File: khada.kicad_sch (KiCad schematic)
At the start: 52 parts, among them J1 MJ-4PP-9, SW1 SW_Push, SW10 SW_Push, SW11 SW_Push, SW12 SW_Push, SW13 SW_Push, SW14 SW_Push, SW15 SW_Push, SW16 SW_Push, SW17 SW_Push, SW18 SW_Push, SW19 SW_Push, SW2 SW_Push, SW20 SW_Push, SW21 SW_Push, SW22 SW_Push, SW3 SW_Push, SW4 SW_Push, SW5 SW_Push, SW6 SW_Push, SW7 SW_Push, SW8 SW_Push, SW9 SW_Push, U1 YAAJ_WeAct_BlackPill_Part_Lik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

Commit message: final design unless wiring incorrect
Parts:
- SW1, SW10, SW12, SW13, SW14, SW15, SW16, SW17, SW18, SW19, SW2, SW20, SW21, SW22, SW3, SW4, SW5: footprint MX_Only:MXOnly-1U-NoLED -> switches:SW_MX_reversible_NoSilk
- SW11, SW6, SW7, SW8, SW9: footprint mx_only:MXOnly-1U-NoLED -> switches:SW_MX_reversible_NoSilk

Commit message: added encoder
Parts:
- added D23: D_Small, acheron_Components:D_THT_7.62mm_copy, symbol Device:D_Small
- added SW23: RotaryEncoder_Switch, keebio:RotaryEncoder_Alps_EC11E-Switch_Vertical_H20mm, symbol Device:RotaryEncoder_Switch
- renumbered D9 to D10, D14 to D11, D11 to D12, D12 to D13, D13 to D14, D18 to D15, D15 to D16, D16 to D17, D17 to D18, D22 to D19, D19 to D20, D20 to D21, D21 to D22, D10 to D7, D7 to D8, D8 to D9, SW9 to SW10, SW14 to SW11, SW11 to SW12, SW12 to SW13, SW13 to SW14, SW18 to SW15, SW15 to SW16, SW16 to SW17, SW17 to SW18, SW22 to SW19, SW19 to SW20, SW20 to SW21, SW21 to SW22, SW10 to SW7, SW7 to SW8, SW8 to SW9
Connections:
- net +5V: now also R1.1; no longer R1.2
- net DATA: now also J1.B, R1.2, U1.10 (PA15); no longer J1.A, R1.1, U1.17 (PB9)
- net GND: now also SW23.C
- net col0: now also U1.5 (PA8); no longer U1.10 (PA15)
- net col1: now also SW7.2
- net col2: now also SW11.2; no longer SW7.2
- net col3: now also SW15.2; no longer SW11.2
- net col4: now also SW19.2; no longer SW15.2
- net col5: now also SW23.S2; no longer SW19.2
- net row3: now also D23.1 (K)
- net ROTA: now reaches U1.16 (PB8)
- net ROTA: now also SW23.A
- new net: D23.2 (A), SW23.S1
- new net ROTB: SW23.B, U1.17 (PB9)
- no-connect marks 1 -> 0
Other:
- moved on the sheet: D11, D15, D19, D7, J1, R1, SW11, SW15, SW19, SW7

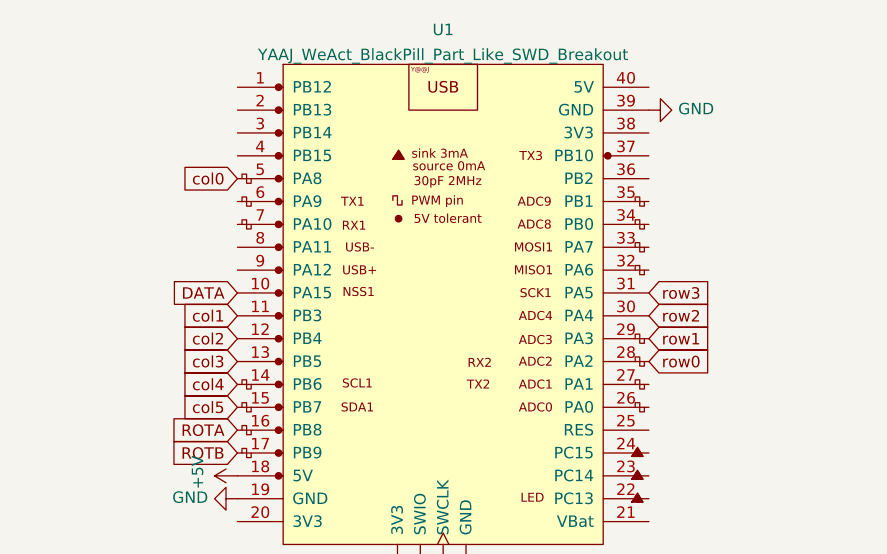
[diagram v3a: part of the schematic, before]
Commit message: edited switch footprint to have pads on both sides
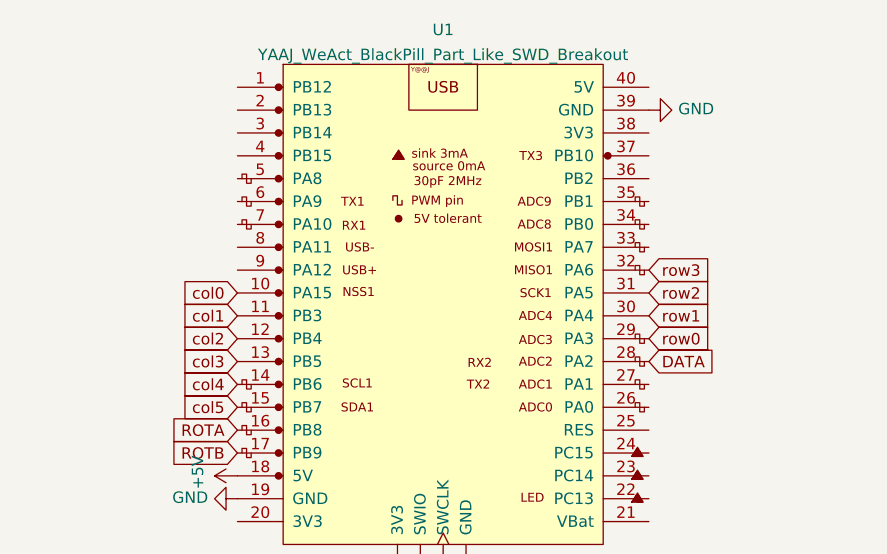
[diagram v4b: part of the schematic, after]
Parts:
- SW1, SW10, SW11, SW12, SW13, SW14, SW15, SW16, SW17, SW18, SW19, SW2, SW20, SW21, SW22, SW3, SW4, SW5, SW6, SW7, SW8, SW9: footprint switches:SW_MX_reversible_NoSilk -> marbastlib-mx:SW_MX_Reversible_1u_PadsOnBothLayers
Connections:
- net DATA: now also U1.28 (PA2); no longer U1.10 (PA15)
- net col0: now also U1.10 (PA15); no longer U1.5 (PA8)
- net row0: now also U1.29 (PA3); no longer U1.28 (PA2)
- net row1: now also U1.30 (PA4); no longer U1.29 (PA3)
- net row2: now also U1.31 (PA5); no longer U1.30 (PA4)
- net row3: now also U1.32 (PA6); no longer U1.31 (PA5)
